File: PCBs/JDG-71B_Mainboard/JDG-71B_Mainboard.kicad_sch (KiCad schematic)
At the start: 1 part, among them U1 Compute_Module_5_Functional

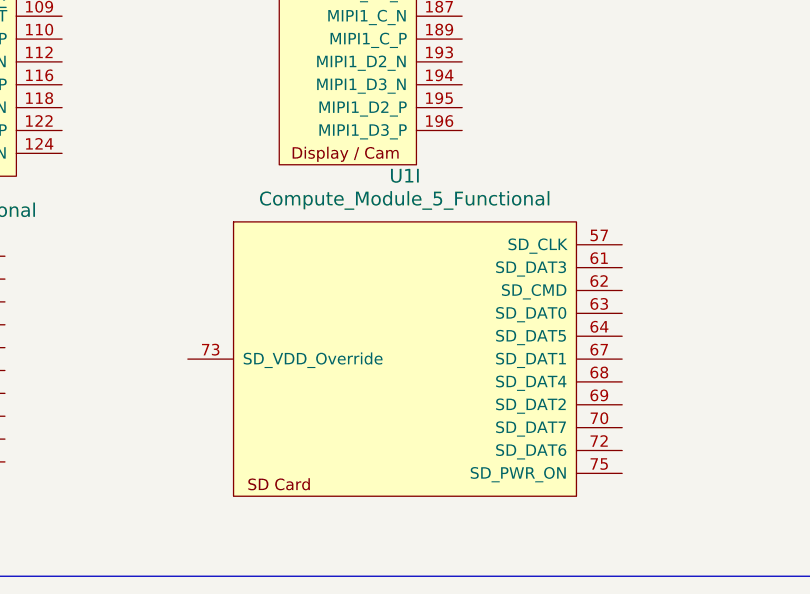
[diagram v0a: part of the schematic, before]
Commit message: updated architecure
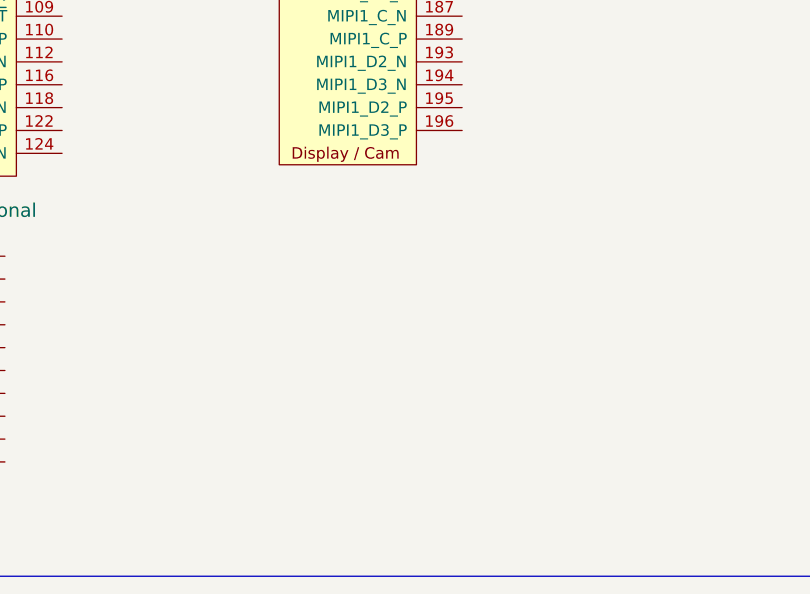
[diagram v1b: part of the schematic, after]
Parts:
- removed unit 9 of U1
